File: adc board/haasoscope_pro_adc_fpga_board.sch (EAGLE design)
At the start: 564 parts, among them CN2 12Vin, IC1 ADC12DL2500ACF, IC13 LMH5401IRMST, IC14 LMH6401IRMZR, IC15 SN74AVC4T774PWR, IC17 DAC8562SDGSR, IC18 TLV9102IPWR, IC2 SN74AVC4T774PWR, IC21 LMH5401IRMST, IC22 TPS7A7200RGTR, IC23 TPS7A7200RGTR, IC24 TPS7A7200RGTR, IC25 TPS72325DBVR, IC26 TPS7A7200RGTR, IC27 TPS7A7200RGTR, IC28 TPS7A7200RGTR, IC29 LMH6401IRMZR, IC3 ADC122S021CIMM_NOPB, IC30 SN74AVC4T774PWR, IC33 TLV9102IPWR, IC4 TLV9102IPWR, IC5 EP4CE30F23C6N, IC6 EPCQ16ASI8N, IC8 FT232HQ, IC9 93LC56B, J1 2p-2.54, J10 8pin, J11 8pin, J13 8pin, J14 2x5, J15 test1, J2 test1, J30 2p-2.54, J31 2p-2.54, J32 2p-2.54, J33 2p-2.54, J34 2p-2.54, J35 2p-2.54, J36 2p-2.54, J37 2p-2.54, J39 2p-2.54, J40 2p-2.54, J41 2p-2.54, J42 2p-2.54, J43 2p-2.54, J44 2p-2.54, J45 2p-2.54, J46 2p-2.54, J8 8pin, K10 G6K-2F-RF-DC3, K11 G6K-2F-RF-DC3, K12 G6K-2F-RF-DC3, K5 AQY21SOP, K6 G6K-2F-RF-DC3, K7 G6K-2F-RF-DC3, K9 AQY21SOP, Q1 S8050, Q4 S8050, Q5 S8050, Q7 S8050, Q8 S8050, Q9 S8050, SW3 SKQGADE010, SW4 SKQGADE010, U2 ADF4350BCPZ, U6 AMS1117-1.2, X1 USBC, Y2 OSCILLATORSMD-5X3, Y3 12MHz

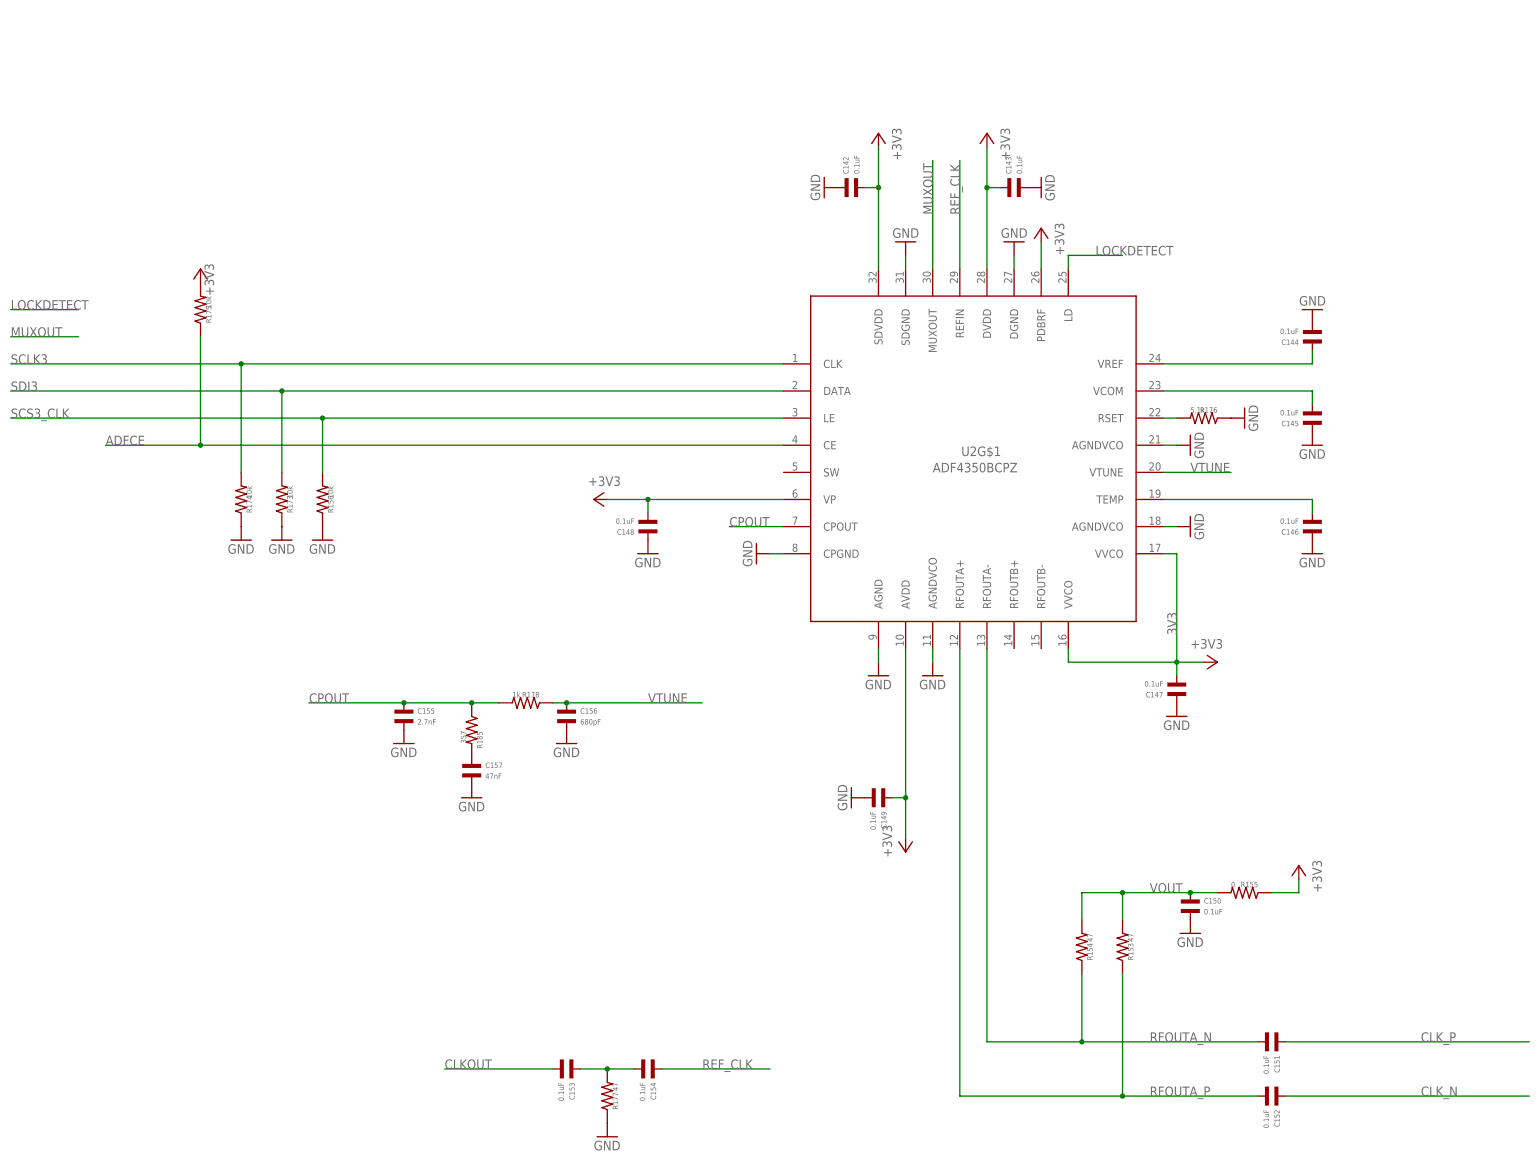
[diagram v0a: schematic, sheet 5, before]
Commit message: remove clk cap
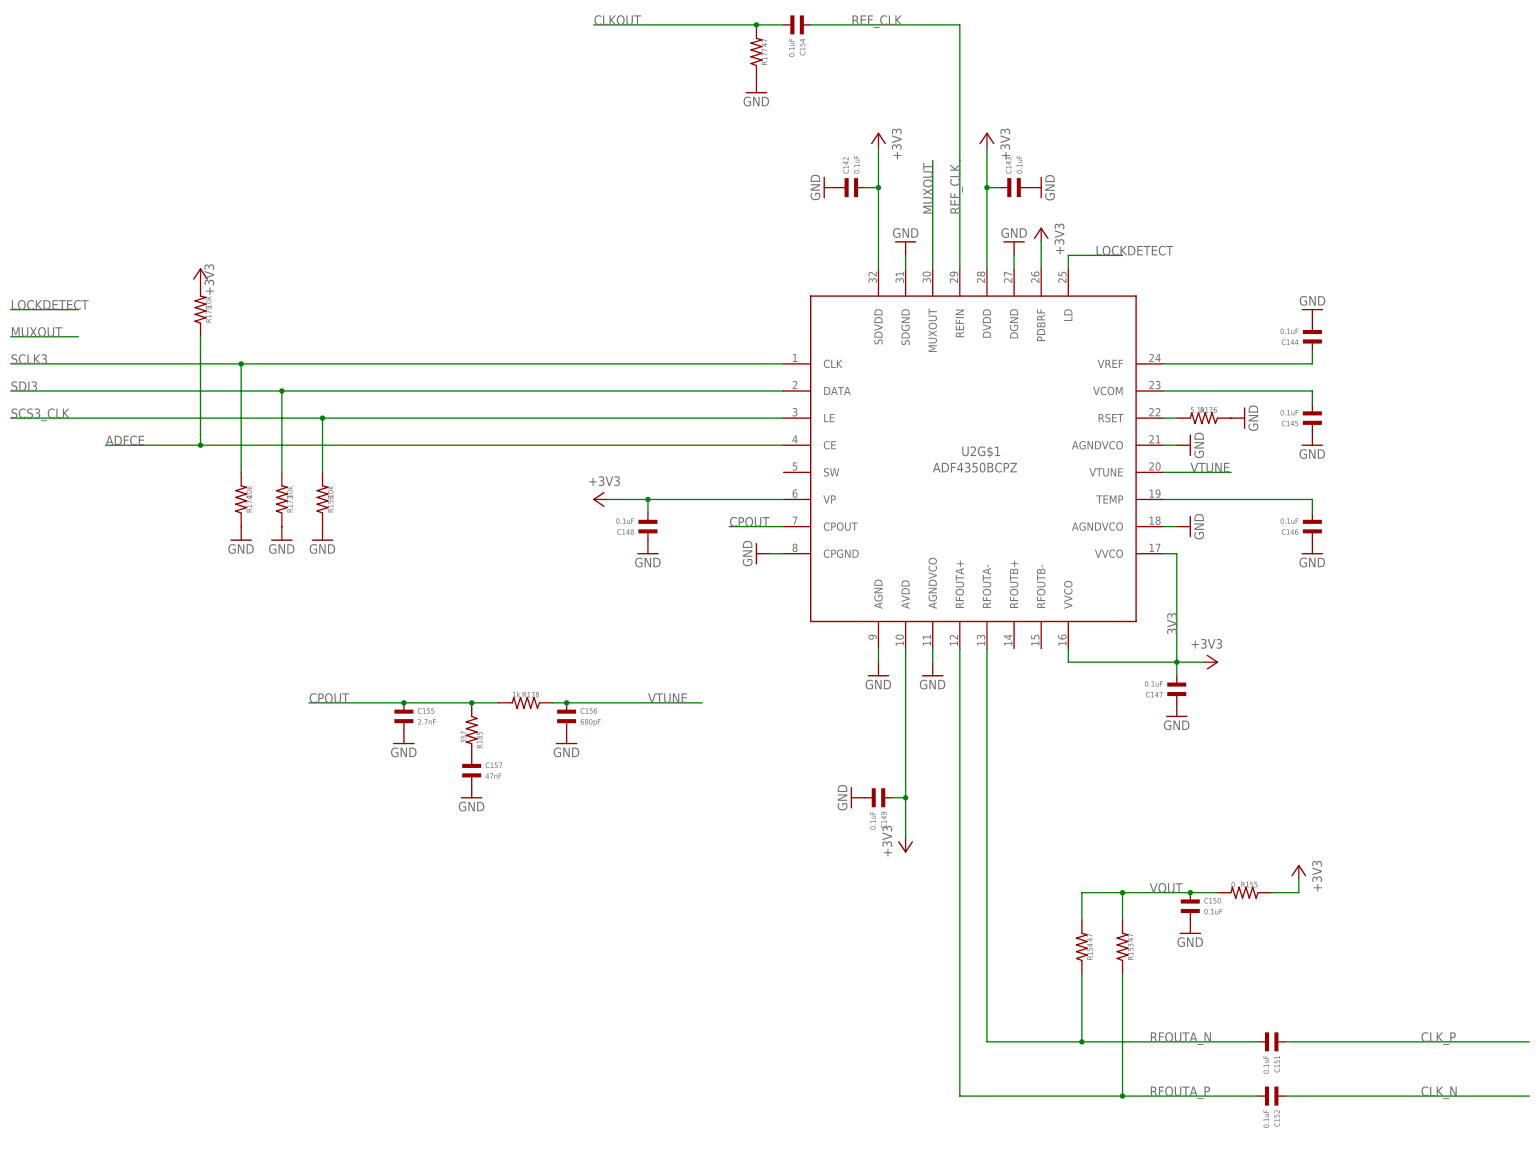
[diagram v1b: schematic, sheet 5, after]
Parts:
- removed C153: 0.1uF, MF_Passives:CAPACITOR_NP_0402
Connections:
- removed net N$23: C153.P$1, C154.P$2, R177.P$2
- net CLKOUT: now also C154.P$2, R177.P$2; no longer C153.P$2
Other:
- moved on the sheet: C154, R177
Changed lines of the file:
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@@
 <part name="C151" library="MF_Passives" deviceset="CAPACITOR_NP" device="_0402" value="0.1uF"/>
 <part name="C152" library="MF_Passives" deviceset="CAPACITOR_NP" device="_0402" value="0.1uF"/>
-<part name="C153" library="MF_Passives" deviceset="CAPACITOR_NP" device="_0402" value="0.1uF"/>
 <part name="R177" library="MF_Passives" deviceset="RESISTOR" device="_0402" value="47"/>
 <part name="GND170" library="supply1" deviceset="GND" device=""/>
@@
 <attribute name="VALUE" x="262.636" y="22.86" size="1.016" layer="96" font="vector" rot="R270"/>
 </instance>
-<instance part="C153" gate="G$1" x="132.08" y="30.48" smashed="yes" rot="R270">
-<attribute name="NAME" x="133.604" y="27.94" size="1.016" layer="95" font="vector" rot="R270" align="top-left"/>
-<attribute name="VALUE" x="130.556" y="27.94" size="1.016" layer="96" font="vector" rot="R270"/>
-</instance>
-<instance part="R177" gate="G$1" x="139.7" y="25.4" smashed="yes" rot="R180">
-<attribute name="NAME" x="140.716" y="22.86" size="1.016" layer="95" font="vector" rot="R90" align="top-left"/>
-<attribute name="VALUE" x="140.716" y="27.94" size="1.016" layer="96" font="vector" rot="R270"/>
-</instance>
-<instance part="GND170" gate="1" x="139.7" y="17.78" smashed="yes">
-<attribute name="VALUE" x="137.16" y="15.24" size="1.778" layer="96"/>
-</instance>
-<instance part="C154" gate="G$1" x="147.32" y="30.48" smashed="yes" rot="R270">
-<attribute name="NAME" x="148.844" y="27.94" size="1.016" layer="95" font="vector" rot="R270" align="top-left"/>
-<attribute name="VALUE" x="145.796" y="27.94" size="1.016" layer="96" font="vector" rot="R270"/>
+<instance part="R177" gate="G$1" x="167.64" y="220.98" smashed="yes" rot="R180">
+<attribute name="NAME" x="168.656" y="218.44" size="1.016" layer="95" font="vector" rot="R90" align="top-left"/>
+<attribute name="VALUE" x="168.656" y="223.52" size="1.016" layer="96" font="vector" rot="R270"/>
+</instance>
+<instance part="GND170" gate="1" x="167.64" y="213.36" smashed="yes">
+<attribute name="VALUE" x="165.1" y="210.82" size="1.778" layer="96"/>
+</instance>
+<instance part="C154" gate="G$1" x="175.26" y="226.06" smashed="yes" rot="R270">
+<attribute name="NAME" x="176.784" y="223.52" size="1.016" layer="95" font="vector" rot="R270" align="top-left"/>
+<attribute name="VALUE" x="173.736" y="223.52" size="1.016" layer="96" font="vector" rot="R270"/>
 </instance>
 <instance part="C155" gate="G$1" x="101.6" y="96.52" smashed="yes">
@@
 <net name="REF_CLK" class="0">
 <segment>
-<wire x1="205.74" y1="200.66" x2="205.74" y2="180.34" width="0.1524" layer="91"/>
+<pinref part="C154" gate="G$1" pin="P$1"/>
+<wire x1="177.8" y1="226.06" x2="205.74" y2="226.06" width="0.1524" layer="91"/>
+<label x="185.42" y="226.06" size="1.778" layer="95"/>
+<wire x1="205.74" y1="200.66" x2="205.74" y2="198.12" width="0.1524" layer="91"/>
 <label x="205.74" y="190.5" size="1.778" layer="95" rot="R90"/>
 <pinref part="U2" gate="G$1" pin="REFIN"/>
-</segment>
-<segment>
-<pinref part="C154" gate="G$1" pin="P$1"/>
-<wire x1="149.86" y1="30.48" x2="170.18" y2="30.48" width="0.1524" layer="91"/>
-<label x="157.48" y="30.48" size="1.778" layer="95"/>
+<wire x1="205.74" y1="198.12" x2="205.74" y2="180.34" width="0.1524" layer="91"/>
+<wire x1="205.74" y1="226.06" x2="205.74" y2="200.66" width="0.1524" layer="91"/>
 </segment>
 </net>
@@
 <net name="CLKOUT" class="5">
 <segment>
-<wire x1="109.22" y1="30.48" x2="129.54" y2="30.48" width="0.1524" layer="91"/>
-<pinref part="C153" gate="G$1" pin="P$2"/>
-<label x="109.22" y="30.48" size="1.778" layer="95"/>
-</segment>
-</net>
-<net name="N$23" class="0">
-<segment>
-<pinref part="C153" gate="G$1" pin="P$1"/>
+<wire x1="137.16" y1="226.06" x2="167.64" y2="226.06" width="0.1524" layer="91"/>
+<label x="137.16" y="226.06" size="1.778" layer="95"/>
 <pinref part="R177" gate="G$1" pin="P$2"/>
-<wire x1="134.62" y1="30.48" x2="139.7" y2="30.48" width="0.1524" layer="91"/>
 <pinref part="C154" gate="G$1" pin="P$2"/>
-<wire x1="139.7" y1="30.48" x2="144.78" y2="30.48" width="0.1524" layer="91"/>
-<junction x="139.7" y="30.48"/>
+<wire x1="167.64" y1="226.06" x2="172.72" y2="226.06" width="0.1524" layer="91"/>
+<junction x="167.64" y="226.06"/>
 </segment>
 </net>

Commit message: put back clk cap
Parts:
- added C51: 0.1uF, MF_Passives:CAPACITOR_NP_0402
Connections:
- new net N$11: C154.P$2, C51.P$1, R177.P$2
- net CLKOUT: now also C51.P$2; no longer C154.P$2, R177.P$2
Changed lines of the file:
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@@
 <part name="R208" library="MF_Passives" deviceset="RESISTOR" device="_0402" value="1k"/>
 <part name="JST_FAN" library="SparkFun-Connectors" deviceset="M02" device="PTH" value="Fan"/>
+<part name="C51" library="MF_Passives" deviceset="CAPACITOR_NP" device="_0402" value="0.1uF"/>
 </parts>
 <sheets>
@@
 <attribute name="VALUE" x="111.76" y="78.74" size="1.778" layer="96"/>
 </instance>
+<instance part="C51" gate="G$1" x="160.02" y="226.06" smashed="yes" rot="R270">
+<attribute name="NAME" x="161.544" y="223.52" size="1.016" layer="95" font="vector" rot="R270" align="top-left"/>
+<attribute name="VALUE" x="158.496" y="223.52" size="1.016" layer="96" font="vector" rot="R270"/>
+</instance>
 </instances>
 <busses>
@@
 <net name="CLKOUT" class="5">
 <segment>
-<wire x1="137.16" y1="226.06" x2="167.64" y2="226.06" width="0.1524" layer="91"/>
 <label x="137.16" y="226.06" size="1.778" layer="95"/>
-<pinref part="R177" gate="G$1" pin="P$2"/>
-<pinref part="C154" gate="G$1" pin="P$2"/>
-<wire x1="167.64" y1="226.06" x2="172.72" y2="226.06" width="0.1524" layer="91"/>
-<junction x="167.64" y="226.06"/>
+<wire x1="137.16" y1="226.06" x2="157.48" y2="226.06" width="0.1524" layer="91"/>
+<pinref part="C51" gate="G$1" pin="P$2"/>
 </segment>
 </net>
@@
 </segment>
 </net>
+<net name="N$11" class="5">
+<segment>
+<pinref part="C154" gate="G$1" pin="P$2"/>
+<pinref part="R177" gate="G$1" pin="P$2"/>
+<wire x1="167.64" y1="226.06" x2="172.72" y2="226.06" width="0.1524" layer="91"/>
+<junction x="167.64" y="226.06"/>
+<wire x1="162.56" y1="226.06" x2="167.64" y2="226.06" width="0.1524" layer="91"/>
+<pinref part="C51" gate="G$1" pin="P$1"/>
+</segment>
+</net>

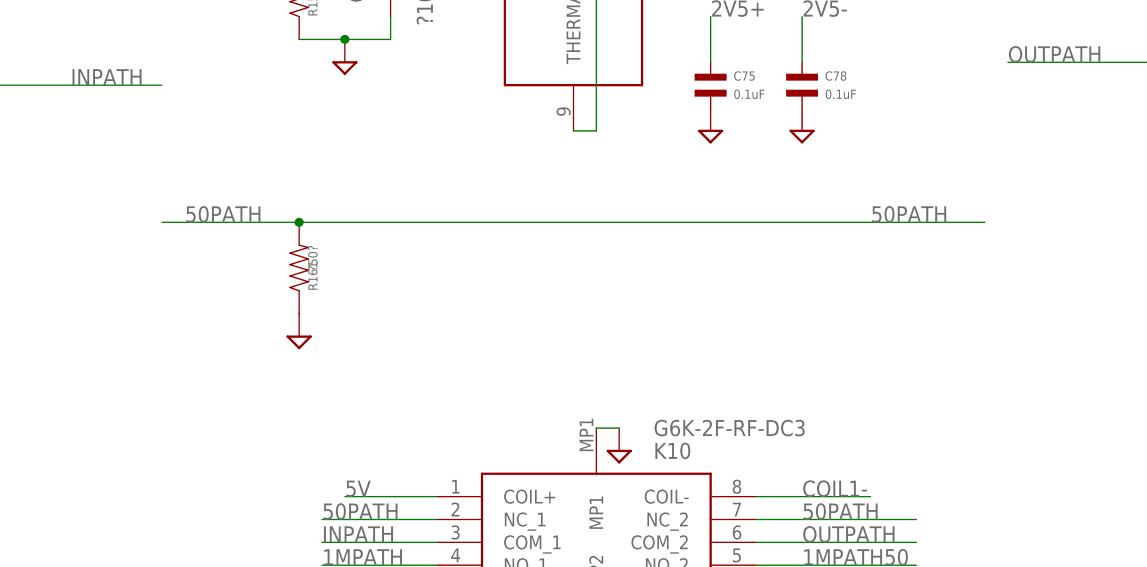
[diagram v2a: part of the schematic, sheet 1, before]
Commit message: remove "50ohm?" pads (causing BW drop at 2 GHz)
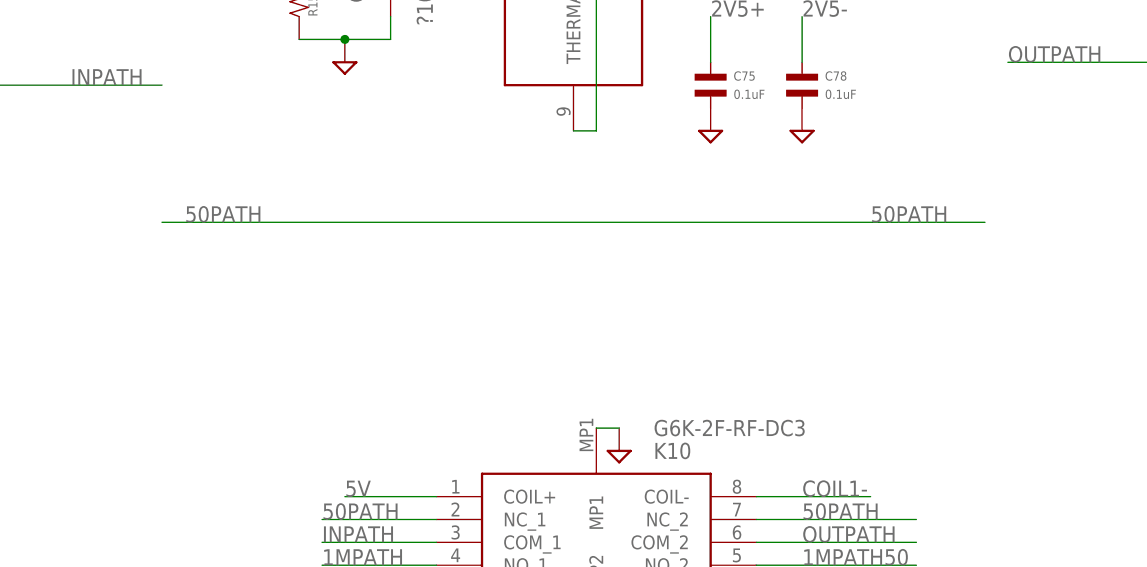
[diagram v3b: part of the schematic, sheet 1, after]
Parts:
- removed R137, R161: ?50?, MF_Passives:RESISTOR_0402
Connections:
- net 50PATH: no longer R161.P$2
- net 50PATH2: no longer R137.P$2
- net GND: no longer R137.P$1, R161.P$1
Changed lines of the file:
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@@
 <part name="SUPPLY86" library="supply2" library_urn="urn:adsk.eagle:library:372" deviceset="GND" device=""/>
 <part name="SUPPLY87" library="supply2" library_urn="urn:adsk.eagle:library:372" deviceset="GND" device=""/>
-<part name="SUPPLY88" library="supply2" library_urn="urn:adsk.eagle:library:372" deviceset="GND" device=""/>
 <part name="Q7" library="Seeed-Transistor" library_urn="urn:adsk.eagle:library:477" deviceset="SMD-TRANSISTORS-NPN-25V-500MW-S8050(SOT-23)" device="" package3d_urn="urn:adsk.eagle:package:33015/1" value="S8050">
 <attribute name="LCSC" value="C7420370"/>
@@
 <part name="SUPPLY41" library="supply2" library_urn="urn:adsk.eagle:library:372" deviceset="GND" device=""/>
 <part name="SUPPLY42" library="supply2" library_urn="urn:adsk.eagle:library:372" deviceset="GND" device=""/>
-<part name="SUPPLY43" library="supply2" library_urn="urn:adsk.eagle:library:372" deviceset="GND" device=""/>
 <part name="Q4" library="Seeed-Transistor" library_urn="urn:adsk.eagle:library:477" deviceset="SMD-TRANSISTORS-NPN-25V-500MW-S8050(SOT-23)" device="" package3d_urn="urn:adsk.eagle:package:33015/1" value="S8050">
 <attribute name="LCSC" value="C7420370"/>
@@
 <part name="R205" library="FlashPCB_Resistors" deviceset="RES-0402" device="" value="1M"/>
 <part name="R42" library="MF_Passives" deviceset="RESISTOR" device="_0402" value="1M"/>
-<part name="R137" library="MF_Passives" deviceset="RESISTOR" device="_0402" value="?50?"/>
 <part name="R158" library="MF_Passives" deviceset="RESISTOR" device="_0402" value="1M"/>
-<part name="R161" library="MF_Passives" deviceset="RESISTOR" device="_0402" value="?50?"/>
 <part name="LED1" library="adafruit" deviceset="LED" device="CHIP-LED0603" package3d_urn="urn:adsk.eagle:package:6240556/1" value="red"/>
 <part name="LED2" library="adafruit" deviceset="LED" device="CHIP-LED0603" package3d_urn="urn:adsk.eagle:package:6240556/1" value="red"/>
@@
 <instance part="SUPPLY86" gate="GND" x="271.78" y="259.08" smashed="yes" rot="MR0"/>
 <instance part="SUPPLY87" gate="GND" x="96.52" y="157.48" smashed="yes"/>
-<instance part="SUPPLY88" gate="GND" x="63.5" y="195.58" smashed="yes" rot="MR0"/>
 <instance part="Q7" gate="G$1" x="99.06" y="137.16" smashed="yes">
 <attribute name="NAME" x="96.52" y="139.7" size="1.27" layer="95" ratio="10"/>
@@
 <attribute name="NAME" x="64.516" y="231.14" size="1.016" layer="95" font="vector" rot="R90" align="top-left"/>
 <attribute name="VALUE" x="64.516" y="236.22" size="1.016" layer="96" font="vector" rot="R270"/>
-</instance>
-<instance part="R161" gate="G$1" x="63.5" y="203.2" smashed="yes" rot="R180">
-<attribute name="NAME" x="64.516" y="200.66" size="1.016" layer="95" font="vector" rot="R90" align="top-left"/>
-<attribute name="VALUE" x="64.516" y="205.74" size="1.016" layer="96" font="vector" rot="R270"/>
 </instance>
 </instances>
@@
 <junction x="424.18" y="261.62"/>
 </segment>
-<segment>
-<pinref part="SUPPLY88" gate="GND" pin="GND"/>
-<pinref part="R161" gate="G$1" pin="P$1"/>
-</segment>
 </net>
 <net name="2V5+" class="1">
@@
 <net name="50PATH" class="0">
 <segment>
-<wire x1="48.26" y1="208.28" x2="63.5" y2="208.28" width="0.1524" layer="91"/>
 <label x="50.8" y="208.28" size="1.778" layer="95"/>
 <label x="127" y="208.28" size="1.778" layer="95"/>
-<pinref part="R161" gate="G$1" pin="P$2"/>
-<wire x1="63.5" y1="208.28" x2="139.7" y2="208.28" width="0.1524" layer="91"/>
-<junction x="63.5" y="208.28"/>
+<wire x1="48.26" y1="208.28" x2="139.7" y2="208.28" width="0.1524" layer="91"/>
 </segment>
 <segment>
@@
 <instance part="SUPPLY41" gate="GND" x="243.84" y="218.44" smashed="yes" rot="MR0"/>
 <instance part="SUPPLY42" gate="GND" x="68.58" y="116.84" smashed="yes"/>
-<instance part="SUPPLY43" gate="GND" x="35.56" y="154.94" smashed="yes" rot="MR0"/>
 <instance part="Q4" gate="G$1" x="71.12" y="96.52" smashed="yes">
 <attribute name="NAME" x="68.58" y="99.06" size="1.27" layer="95" ratio="10"/>
@@
 <attribute name="NAME" x="36.576" y="190.5" size="1.016" layer="95" font="vector" rot="R90" align="top-left"/>
 <attribute name="VALUE" x="36.576" y="195.58" size="1.016" layer="96" font="vector" rot="R270"/>
-</instance>
-<instance part="R137" gate="G$1" x="35.56" y="162.56" smashed="yes" rot="R180">
-<attribute name="NAME" x="36.576" y="160.02" size="1.016" layer="95" font="vector" rot="R90" align="top-left"/>
-<attribute name="VALUE" x="36.576" y="165.1" size="1.016" layer="96" font="vector" rot="R270"/>
 </instance>
 </instances>
@@
 <pinref part="SUPPLY60" gate="GND" pin="GND"/>
 <pinref part="J2" gate="G$1" pin="GND"/>
-</segment>
-<segment>
-<pinref part="SUPPLY43" gate="GND" pin="GND"/>
-<pinref part="R137" gate="G$1" pin="P$1"/>
 </segment>
 </net>
@@
 <net name="50PATH2" class="0">
 <segment>
-<wire x1="20.32" y1="167.64" x2="35.56" y2="167.64" width="0.1524" layer="91"/>
 <label x="22.86" y="167.64" size="1.778" layer="95"/>
 <label x="99.06" y="167.64" size="1.778" layer="95"/>
-<pinref part="R137" gate="G$1" pin="P$2"/>
-<wire x1="35.56" y1="167.64" x2="111.76" y2="167.64" width="0.1524" layer="91"/>
-<junction x="35.56" y="167.64"/>
-</segment>
-<segment>
+<wire x1="20.32" y1="167.64" x2="111.76" y2="167.64" width="0.1524" layer="91"/>
+</segment>
+<segment>
